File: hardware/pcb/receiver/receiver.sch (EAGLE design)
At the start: 79 parts, among them X1 5-1634506-1H

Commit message: hw: board updates
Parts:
- SV1: MFR 929975-01-20 -> (none)
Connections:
- removed net N$34: SV1.GPIO_01
- new net N$32: SV1.GPIO_029
- new net N$35: SV1.GPIO_031
- new net N$36: SV1.GPIO_033
- new net N$37: SV1.GPIO_032
- new net N$38: SV1.GPIO_030
- new net N$45: SV1.GPIO_028
- new net N$46: SV1.GPIO_026
- new net N$48: SV1.VCC3P3
- new net N$52: SV1.GPIO_02
- new net N$58: SV1.VCC_SYS
- net DA0: now also SV1.GPIO_08
- net DA1: now also SV1.GPIO_09
- net DA10: now also SV1.GPIO_018
- net DA11: now also SV1.GPIO_019
- net DA12: now also SV1.GPIO_020
- net DA13: now also SV1.GPIO_021
- net DA14: now also SV1.GPIO_022
- net DA15: now also SV1.GPIO_023
- net DA2: now also SV1.GPIO_010
- net DA3: now also SV1.GPIO_011
- net DA4: now also SV1.GPIO_012
- net DA5: now also SV1.GPIO_013
- net DA6: now also SV1.GPIO_014
- net DA7: now also SV1.GPIO_015
- net DA8: now also SV1.GPIO_016
- net DA9: now also SV1.GPIO_017
- net DITH: now also SV1.GPIO_01
- net GND: now also SV1.GND1, SV1.GND2; no longer SV1.GND
- net OFA: now also SV1.GPIO_025
- net PGA: now also SV1.GPIO_027
- net RAND: now also SV1.GPIO_024

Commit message: hw: ground plane
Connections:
- net N$20 renamed 12-18V
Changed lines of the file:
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@@
 </segment>
 </net>
-<net name="N$20" class="0">
+<net name="12-18V" class="0">
 <segment>
 <pinref part="D2" gate="G$1" pin="A"/>

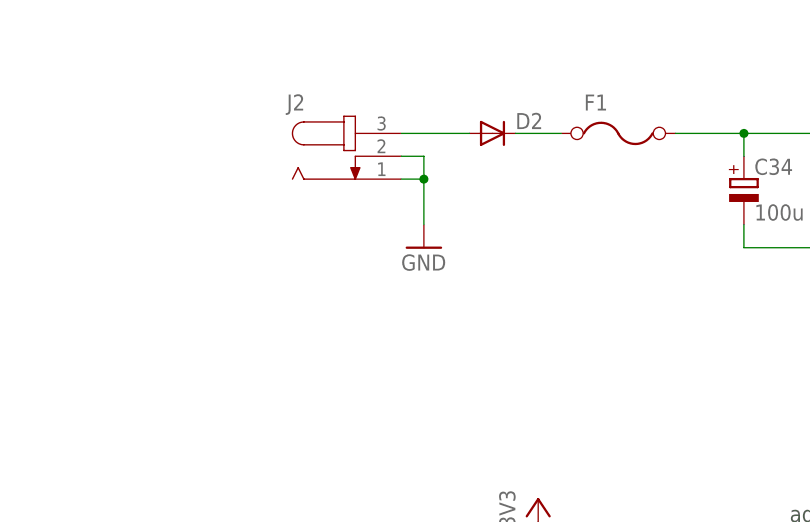
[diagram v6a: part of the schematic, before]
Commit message: hw: added optional mta100
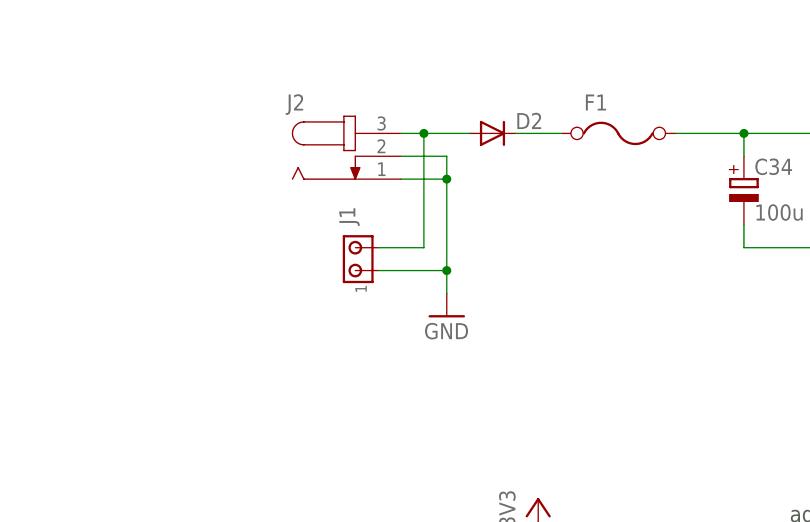
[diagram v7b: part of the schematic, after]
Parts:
- added J1: (no value), con-amp:MTA02-100
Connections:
- net 12-18V: now also J1.2
- net GND: now also J1.1
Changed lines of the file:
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@@
 <part name="SUPPLY3" library="supply2" deviceset="VDD" device=""/>
 <part name="SV1" library="lstolcman_thesis" deviceset="PINHEADER" device=""/>
+<part name="J1" library="con-amp" deviceset="MTA02-100" device="">
+<attribute name="MFR" value="640454-2"/>
+<attribute name="SUP" value="tme"/>
+</part>
 </parts>
 <sheets>
@@
 <attribute name="MFR" x="-297.18" y="63.5" size="2.54" layer="96" rot="R90" display="off"/>
 </instance>
-<instance part="GND3" gate="1" x="-269.24" y="269.24"/>
+<instance part="GND3" gate="1" x="-266.7" y="261.62"/>
 <instance part="J2" gate="G$1" x="-276.86" y="279.4">
 <attribute name="MFR" x="-276.86" y="279.4" size="1.778" layer="96" display="off"/>
@@
 <instance part="SUPPLY3" gate="G$1" x="73.66" y="-2.54"/>
 <instance part="SV1" gate="G$1" x="284.48" y="50.8"/>
+<instance part="J1" gate="G$1" x="-276.86" y="266.7" rot="R90">
+<attribute name="MFR" x="-276.86" y="266.7" size="1.27" layer="96" rot="R90" display="off"/>
+<attribute name="SUP" x="-276.86" y="266.7" size="1.27" layer="96" rot="R90" display="off"/>
+</instance>
 </instances>
 <busses>
@@
 <pinref part="GND2" gate="1" pin="GND"/>
 <pinref part="X1" gate="G$1" pin="2"/>
-</segment>
-<segment>
-<pinref part="GND3" gate="1" pin="GND"/>
-<pinref part="J2" gate="G$1" pin="1"/>
-<wire x1="-269.24" y1="276.86" x2="-269.24" y2="271.78" width="0.1524" layer="91"/>
-<wire x1="-271.78" y1="276.86" x2="-269.24" y2="276.86" width="0.1524" layer="91"/>
-<pinref part="J2" gate="G$1" pin="2"/>
-<wire x1="-271.78" y1="279.4" x2="-269.24" y2="279.4" width="0.1524" layer="91"/>
-<wire x1="-269.24" y1="279.4" x2="-269.24" y2="276.86" width="0.1524" layer="91"/>
-<junction x="-269.24" y="276.86"/>
 </segment>
 <segment>
@@
 <pinref part="GND32" gate="1" pin="GND"/>
 <wire x1="73.66" y1="-20.32" x2="73.66" y2="-17.78" width="0.1524" layer="91"/>
+</segment>
+<segment>
+<pinref part="J2" gate="G$1" pin="1"/>
+<wire x1="-271.78" y1="276.86" x2="-266.7" y2="276.86" width="0.1524" layer="91"/>
+<wire x1="-266.7" y1="276.86" x2="-266.7" y2="279.4" width="0.1524" layer="91"/>
+<pinref part="J2" gate="G$1" pin="2"/>
+<wire x1="-266.7" y1="279.4" x2="-271.78" y2="279.4" width="0.1524" layer="91"/>
+<pinref part="GND3" gate="1" pin="GND"/>
+<wire x1="-266.7" y1="276.86" x2="-266.7" y2="266.7" width="0.1524" layer="91"/>
+<junction x="-266.7" y="276.86"/>
+<pinref part="J1" gate="G$1" pin="1"/>
+<wire x1="-266.7" y1="266.7" x2="-266.7" y2="264.16" width="0.1524" layer="91"/>
+<wire x1="-274.32" y1="266.7" x2="-266.7" y2="266.7" width="0.1524" layer="91"/>
+<junction x="-266.7" y="266.7"/>
 </segment>
 </net>
@@
 <pinref part="D2" gate="G$1" pin="A"/>
 <pinref part="J2" gate="G$1" pin="3"/>
-<wire x1="-264.16" y1="281.94" x2="-271.78" y2="281.94" width="0.1524" layer="91"/>
-</segment>
-</net>
+<wire x1="-264.16" y1="281.94" x2="-269.24" y2="281.94" width="0.1524" layer="91"/>
+<pinref part="J1" gate="G$1" pin="2"/>
+<wire x1="-269.24" y1="281.94" x2="-271.78" y2="281.94" width="0.1524" layer="91"/>
+<wire x1="-274.32" y1="269.24" x2="-269.24" y2="269.24" width="0.1524" layer="91"/>
+<wire x1="-269.24" y1="269.24" x2="-269.24" y2="281.94" width="0.1524" layer="91"/>
+<junction x="-269.24" y="281.94"/>
+</segment>
+</net>

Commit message: hw: gnd vias
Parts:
- SV1: MFR (none) -> ZL262-40DG; SUP (none) -> tme
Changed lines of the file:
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@@
 <part name="H4" library="holes" deviceset="MOUNT-HOLE" device="3.3"/>
 <part name="SUPPLY3" library="supply2" deviceset="VDD" device=""/>
-<part name="SV1" library="lstolcman_thesis" deviceset="PINHEADER" device=""/>
+<part name="SV1" library="lstolcman_thesis" deviceset="PINHEADER" device="">
+<attribute name="MFR" value="ZL262-40DG"/>
+<attribute name="SUP" value="tme"/>
+</part>
 <part name="J1" library="con-amp" deviceset="MTA02-100" device="">
 <attribute name="MFR" value="640454-2"/>
@@
 <instance part="H4" gate="G$1" x="-340.36" y="-12.7"/>
 <instance part="SUPPLY3" gate="G$1" x="73.66" y="-2.54"/>
-<instance part="SV1" gate="G$1" x="284.48" y="50.8"/>
+<instance part="SV1" gate="G$1" x="284.48" y="50.8">
+<attribute name="SUP" x="284.48" y="50.8" size="1.27" layer="96" display="off"/>
+<attribute name="MFR" x="284.48" y="50.8" size="1.27" layer="96" display="off"/>
+</instance>
 <instance part="J1" gate="G$1" x="-276.86" y="266.7" rot="R90">
 <attribute name="MFR" x="-276.86" y="266.7" size="1.27" layer="96" rot="R90" display="off"/>
